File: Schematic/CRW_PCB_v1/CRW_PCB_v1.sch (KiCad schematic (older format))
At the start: 3 parts

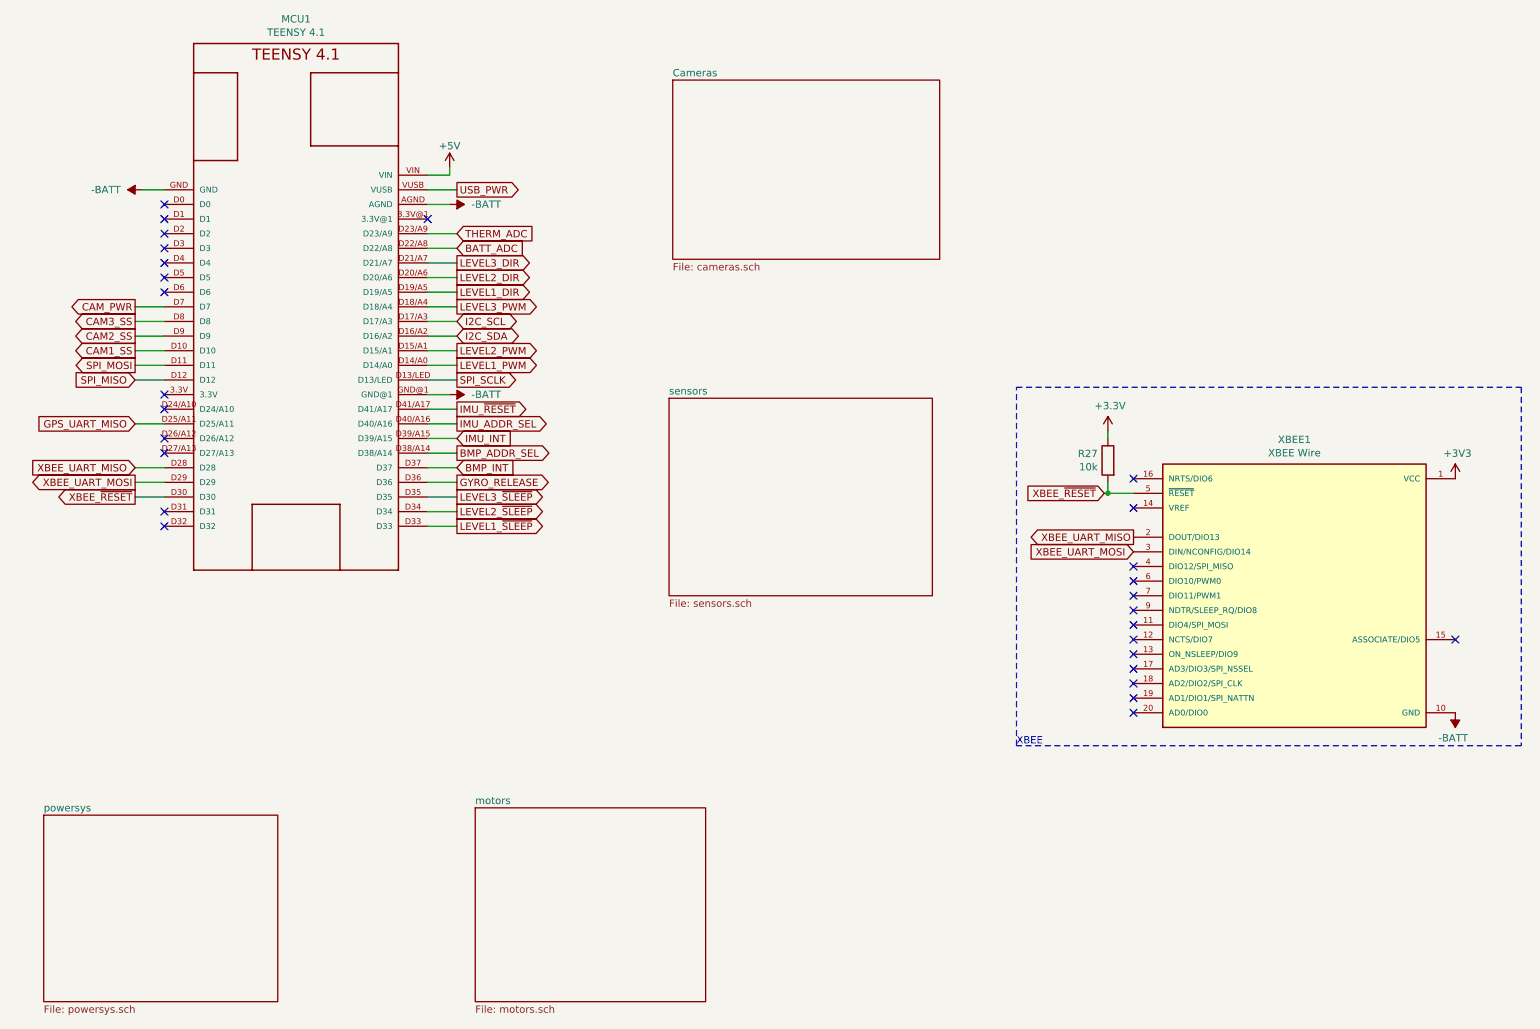
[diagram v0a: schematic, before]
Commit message: Added Hotwire Connection
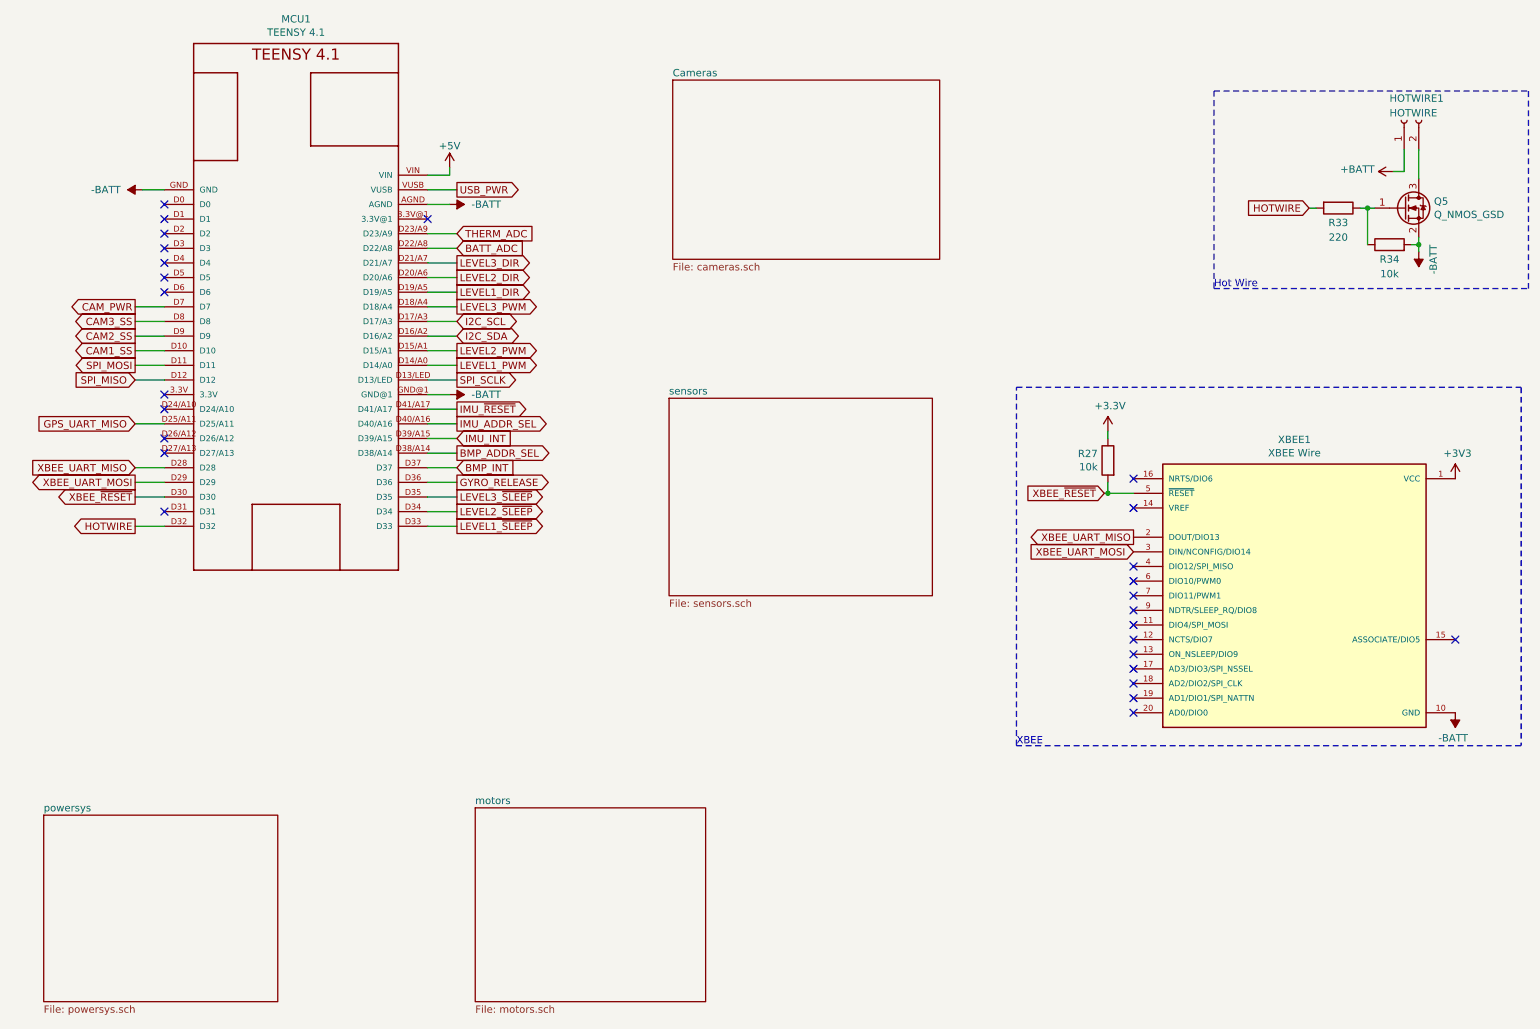
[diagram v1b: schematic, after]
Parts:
- added HOTWIRE1: HOTWIRE, Connector_JST:JST_PH_B2B-PH-K_1x02_P2.00mm_Vertical, symbol Connector:Conn_01x02_Female
- added Q5: Q_NMOS_GSD, Package_TO_SOT_SMD:SC-59_Handsoldering, symbol Device:Q_NMOS_GSD
- added R33: 220, Resistor_SMD:R_0603_1608Metric_Pad0.98x0.95mm_HandSolder, symbol Device:R
- added R34: 10k, Resistor_SMD:R_0402_1005Metric_Pad0.72x0.64mm_HandSolder, symbol Device:R
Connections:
- net -BATT: now also Q5.2 (S), R34.2
- net HOTWIRE: now reaches MCU1.D32
- net HOTWIRE: now also R33.2
- new net: Q5.1 (G), R33.1, R34.1
- new net: HOTWIRE1.2 (Pin_2), Q5.3 (D)
- new net +BATT: HOTWIRE1.1 (Pin_1)
- no-connect marks 28 -> 27
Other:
- note added: "Hot Wire"
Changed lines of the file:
@@
 NoConn ~ 1700 3700
 NoConn ~ 1700 4100
-NoConn ~ 1700 4200
 Wire Wire Line
 	3650 1750 3650 1800
@@
 F1 "cameras.sch" 50
 $EndSheet
+Text GLabel 1500 4200 0    50   Output ~ 0
+HOTWIRE
+Wire Wire Line
+	1500 4200 1700 4200
+$Comp
+L power:-BATT #PWR053
+U 1 1 600901B3
+P 10275 2325
+AR Path="/600901B3" Ref="#PWR053"  Part="1"
+AR Path="/600B1082/600901B3" Ref="#PWR?"  Part="1"
+F 0 "#PWR053" H 10275 2175 50  0001 C CNN
+F 1 "-BATT" V 10175 2275 50  0000 L CNN
+F 2 "" H 10275 2325 50  0001 C CNN
+F 3 "" H 10275 2325 50  0001 C CNN
+	1    10275 2325
+	-1   0    0    1
+$EndComp
+$Comp
+L Device:Q_NMOS_GSD Q5
+U 1 1 600901B9
+P 10175 2025
+AR Path="/600901B9" Ref="Q5"  Part="1"
+AR Path="/600B1082/600901B9" Ref="Q?"  Part="1"
+F 0 "Q5" H 10379 2071 50  0000 L CNN
+F 1 "Q_NMOS_GSD" H 10379 1980 50  0000 L CNN
+F 2 "Package_TO_SOT_SMD:SC-59_Handsoldering" H 10375 2125 50  0001 C CNN
+F 3 "~" H 10175 2025 50  0001 C CNN
+	1    10175 2025
+	1    0    0    -1
+$EndComp
+Wire Wire Line
+	10275 2275 10275 2225
+$Comp
+L Device:R R34
+U 1 1 600901C0
+P 10075 2275
+AR Path="/600901C0" Ref="R34"  Part="1"
+AR Path="/600B1082/600901C0" Ref="R?"  Part="1"
+F 0 "R34" V 9975 2275 50  0000 C CNN
+F 1 "10k" V 9875 2275 50  0000 C CNN
+F 2 "Resistor_SMD:R_0402_1005Metric_Pad0.72x0.64mm_HandSolder" V 10005 2275 50  0001 C CNN
+F 3 "~" H 10075 2275 50  0001 C CNN
+	1    10075 2275
+	0    -1   -1   0
+$EndComp
+Wire Wire Line
+	9925 2275 9925 2025
+Wire Wire Line
+	9925 2025 9975 2025
+Wire Wire Line
+	9925 2025 9875 2025
+Connection ~ 9925 2025
+Wire Wire Line
+	10225 2275 10275 2275
+Wire Wire Line
+	10275 2275 10275 2325
+Connection ~ 10275 2275
+Text GLabel 9525 2025 0    50   Input ~ 0
+HOTWIRE
+$Comp
+L Connector:Conn_01x02_Female HOTWIRE1
+U 1 1 600901CE
+P 10175 1425
+AR Path="/600901CE" Ref="HOTWIRE1"  Part="1"
+AR Path="/600B1082/600901CE" Ref="RELEASE?"  Part="1"
+F 0 "HOTWIRE1" V 10325 1525 50  0000 R CNN
+F 1 "HOTWIRE" V 10225 1525 50  0000 R CNN
+F 2 "Connector_JST:JST_PH_B2B-PH-K_1x02_P2.00mm_Vertical" H 10175 1425 50  0001 C CNN
+F 3 "~" H 10175 1425 50  0001 C CNN
+	1    10175 1425
+	0    -1   -1   0
+$EndComp
+Wire Notes Line
+	11025 1225 11025 2575
+Wire Notes Line
+	8875 2575 8875 1225
+Text Notes 8875 2575 0    50   ~ 0
+Hot Wire
+$Comp
+L Device:R R33
+U 1 1 600901D7
+P 9725 2025
+AR Path="/600901D7" Ref="R33"  Part="1"
+AR Path="/600B1082/600901D7" Ref="R?"  Part="1"
+F 0 "R33" V 9825 2025 50  0000 C CNN
+F 1 "220" V 9925 2025 50  0000 C CNN
+F 2 "Resistor_SMD:R_0603_1608Metric_Pad0.98x0.95mm_HandSolder" V 9655 2025 50  0001 C CNN
+F 3 "~" H 9725 2025 50  0001 C CNN
+	1    9725 2025
+	0    1    1    0
+$EndComp
+Wire Wire Line
+	9525 2025 9575 2025
+Wire Notes Line
+	8875 1225 11025 1225
+Wire Notes Line
+	8875 2575 11025 2575
+Wire Wire Line
+	10275 1625 10275 1825
+Wire Wire Line
+	10100 1775 10175 1775
+$Comp
+L power:+BATT #PWR052
+U 1 1 600901E2
+P 10100 1775
+AR Path="/600901E2" Ref="#PWR052"  Part="1"
+AR Path="/600B1082/600901E2" Ref="#PWR?"  Part="1"
+F 0 "#PWR052" H 10100 1625 50  0001 C CNN
+F 1 "+BATT" V 10115 1902 50  0000 L CNN
+F 2 "" H 10100 1775 50  0001 C CNN
+F 3 "" H 10100 1775 50  0001 C CNN
+	1    10100 1775
+	0    -1   -1   0
+$EndComp
+Wire Wire Line
+	10175 1625 10175 1775
 $EndSCHEMATC
